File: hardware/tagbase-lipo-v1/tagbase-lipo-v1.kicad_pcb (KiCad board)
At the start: 2 copper layers, 50.8 x 69.9 mm, 37 parts, among them J1 Conn_01x04_Female, J101 Conn_02x03_Odd_Even, J102 Conn_02x05_Odd_Even, J104 USB_B_Mini, J2 Conn_01x06, J5 Conn_01x02, SW1 SW_SPDT, SW2 SW_SPDT, U1 XC6206P332MR, U105 Tactile Switch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

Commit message: checkpoint
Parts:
- removed R105: 10K, Resistor_SMD:R_0603_1608Metric
- added C6: 4.7uf, Capacitor_SMD:C_0402_1005Metric, F.Cu at (126.7, 70.3)
- added C7: 4.7uf, Capacitor_SMD:C_0402_1005Metric, F.Cu at (131.1, 63.4)
- C1, C101, C104, C107, C2, C3, C4, C5: footprint Capacitor_SMD:C_0603_1608Metric -> Capacitor_SMD:C_0402_1005Metric
- R1: value 30K -> 33K; footprint Resistor_SMD:R_0603_1608Metric -> Resistor_SMD:R_0402_1005Metric
- R101: value 680 -> 220
- R102: value 680 -> 100
- R104, R2, R3: footprint Resistor_SMD:R_0603_1608Metric -> Resistor_SMD:R_0402_1005Metric
- R107: value 680 -> 300
- U3: value XC6206P182MR -> XC6206P202MR
- moved R2 43.6 mm to (150.3, 77.4), turned to -90 degrees
- moved U2 42.6 mm to (149.3, 74.7), turned to 0 degrees
- moved R1 42.4 mm to (149.0, 77.4), turned to -90 degrees
- moved D105 42.2 mm to (149.9, 69.1)
- moved R107 42.1 mm to (147.8, 69.3)
- moved U105 39.3 mm to (108.7, 59.7), turned to -90 degrees
- moved C5 33.3 mm to (141.4, 63.2)
- moved U3 33.3 mm to (141.3, 60.5)
- moved C4 32.8 mm to (140.8, 57.9), turned to 180 degrees
- moved SW2 30.3 mm to (143.2, 70.1), turned to 90 degrees
- moved R3 24.4 mm to (132.0, 66.2)
- moved C107 13.6 mm to (132.2, 63.4), turned to -90 degrees
- moved J1 13.2 mm to (147.5, 63.3)
- moved C3 9.71 mm to (123.1, 66.6), turned to 180 degrees
- moved SW1 8.91 mm to (143.2, 76.7), turned to 90 degrees
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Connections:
- C2 pad 1: +1V8 -> +2V
- C5 pad 1: +1V8 -> +2V
- J102 pad 4: /SCLK -> /SWCLK
- R3 pad 1: +1V8 -> +3V3
- U105 pad 1: /boot0 -> /SWCLK
- U3 pad 2: +1V8 -> +2V
- U4 pad 16: unconnected-(U4-PA8-Pad16) -> /LED_GREEN
- U4 pad 20: unconnected-(U4-PA13-Pad20) -> /SWDIO
- U4 pad 21: /boot0 -> /SWCLK
- U4 pad 22: unconnected-(U4-PA15-Pad22) -> /LED_RED
- U4 pad 3: +1V8 -> +2V
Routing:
- net +3V3: track 3.52 -> 57.4 mm, vias 1 -> 2
- net /SWCLK: track 0.00 -> 27.6 mm, vias 0 -> 1
- net /CSO: track 0.00 -> 20.4 mm, vias 0 -> 2
- net TAG_3V3_IN: track 0.00 -> 18.6 mm, vias 0 -> 1
- net TAG_VBAT: track 12.0 -> 28.4 mm
- net /LED_GREEN: track 0.00 -> 16.1 mm, vias 0 -> 2
- net /LED_RED: track 2.64 -> 15.6 mm, vias 0 -> 2
- net /SWDIO: track 0.00 -> 12.9 mm
- net VUSB: track 26.7 -> 37.1 mm, vias 1 -> 0
- net TAG_3V3: track 18.2 -> 25.5 mm
- net GND: track 26.1 -> 30.7 mm, vias 9 -> 11
- net /BAT: track 0.00 -> 4.26 mm
- net /USB_DP: track 0.00 -> 3.89 mm
- net Net-(U2-THIN/NF): track 0.00 -> 3.09 mm
- net /NRST: track 2.63 -> 0.00 mm
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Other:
- board text removed: "USB"

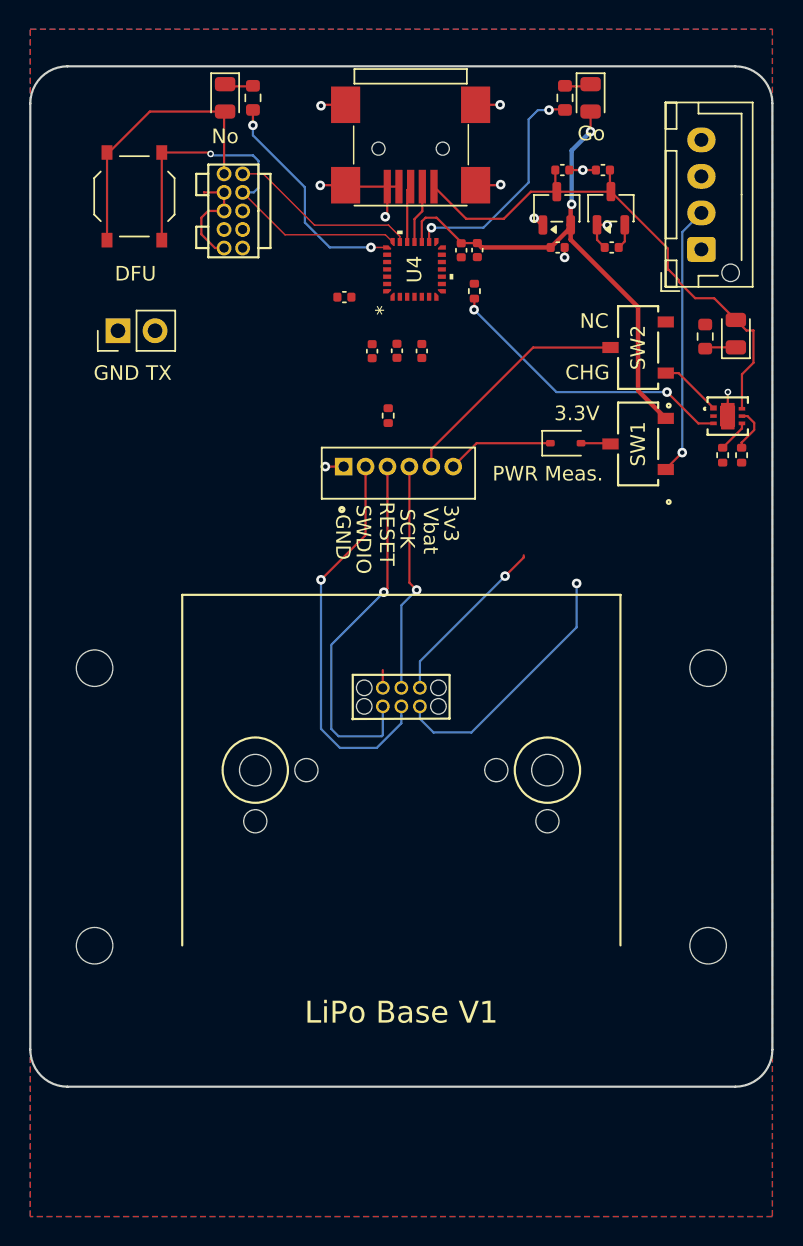
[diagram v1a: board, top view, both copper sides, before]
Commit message: restructure data logging
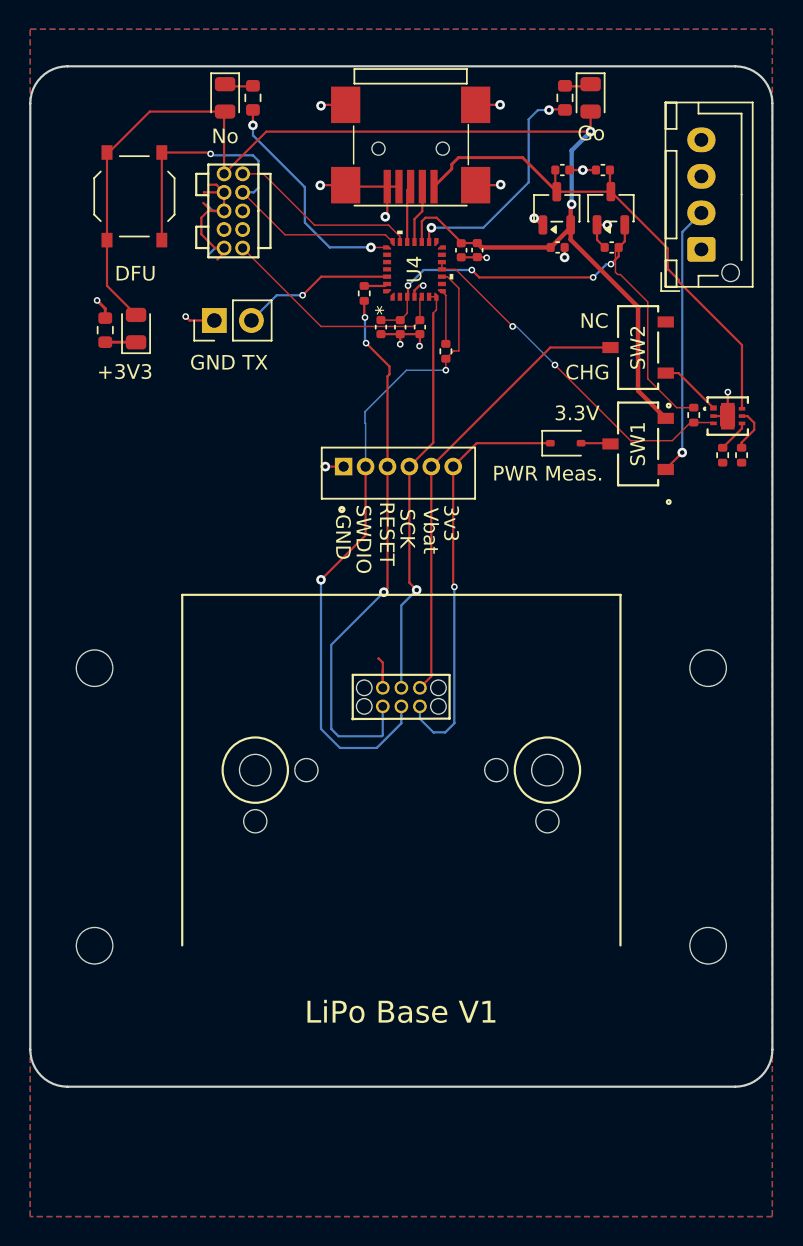
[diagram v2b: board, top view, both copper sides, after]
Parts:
- removed C3: 0.1uF, Capacitor_SMD:C_0402_1005Metric
- removed R107: 300, Resistor_SMD:R_0603_1608Metric
- added R4: 1K, Resistor_SMD:R_0402_1005Metric, F.Cu at (130.0, 70.3)
- added R5: 100, Resistor_SMD:R_0603_1608Metric, F.Cu at (106.7, 68.9)
- moved D105 41.1 mm to (108.8, 68.8)
- moved R3 17.2 mm to (147.0, 74.7)
- moved R104 8.53 mm to (124.5, 66.3)
- moved J5 6.64 mm to (114.2, 68.2)
- moved C2 1.75 mm to (125.6, 68.7)
- moved C101 1.64 mm to (128.3, 68.7)
- moved C6 1.63 mm to (126.9, 68.7)
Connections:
- D105 pad 2: VUSB -> +3V3
- J1 pad 1: TAG_MIRROR -> unconnected-(J1-Pin_1-Pad1)
- J1 pad 3: EXT_PWR -> unconnected-(J1-Pin_3-Pad3)
- R104 pad 2: unconnected-(R104-Pad2) -> Net-(U4-PB7)
- R3 pad 1: +3V3 -> +2V
- U4 pad 10: unconnected-(U4-PA4-Pad10) -> TAG_SWDIO
- U4 pad 11: unconnected-(U4-PA5-Pad11) -> /CSO
- U4 pad 12: unconnected-(U4-PA6-Pad12) -> /CSO
- U4 pad 26: unconnected-(U4-PB6-Pad26) -> /UART_TX
- U4 pad 27: unconnected-(U4-PB7-Pad27) -> Net-(U4-PB7)
- U4 pad 6: unconnected-(U4-PA0-Pad6) -> TAG_SCK
- U4 pad 7: unconnected-(U4-PA1-Pad7) -> TAG_SCK
- U4 pad 8: unconnected-(U4-PA2-Pad8) -> Net-(U4-PA2)
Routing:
- net +2V: track 1.72 -> 36.2 mm, vias 0 -> 4
- net +3V3: track 57.4 -> 89.5 mm
- net GND: track 30.7 -> 51.1 mm, vias 11 -> 17
- net TAG_SWDIO: track 27.1 -> 45.3 mm, vias 1 -> 2
- net /NRST: track 0.00 -> 16.2 mm
- net TAG_SCK: track 15.8 -> 28.7 mm
- net TAG_RESET: track 25.2 -> 37.4 mm, vias 1 -> 3
- net /UART_TX: track 0.00 -> 10.5 mm, vias 0 -> 1
- net /CSO: track 20.4 -> 24.5 mm
- net Net-(U4-PA2): track 0.00 -> 3.71 mm
- net TAG_3V3: track 25.5 -> 28.8 mm
- net TAG_VBAT: track 28.4 -> 31.1 mm, vias 1 -> 0
- net Net-(U4-PB7): track 0.00 -> 1.62 mm
- net VUSB: track 37.1 -> 35.7 mm
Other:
- board text added: "+3V3"
